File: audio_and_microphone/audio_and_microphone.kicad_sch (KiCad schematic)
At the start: 36 parts, among them J2 Conn_01x02, U1 LM4810, U2 ${SIM.PARAMS}, U3 ${SIM.PARAMS}

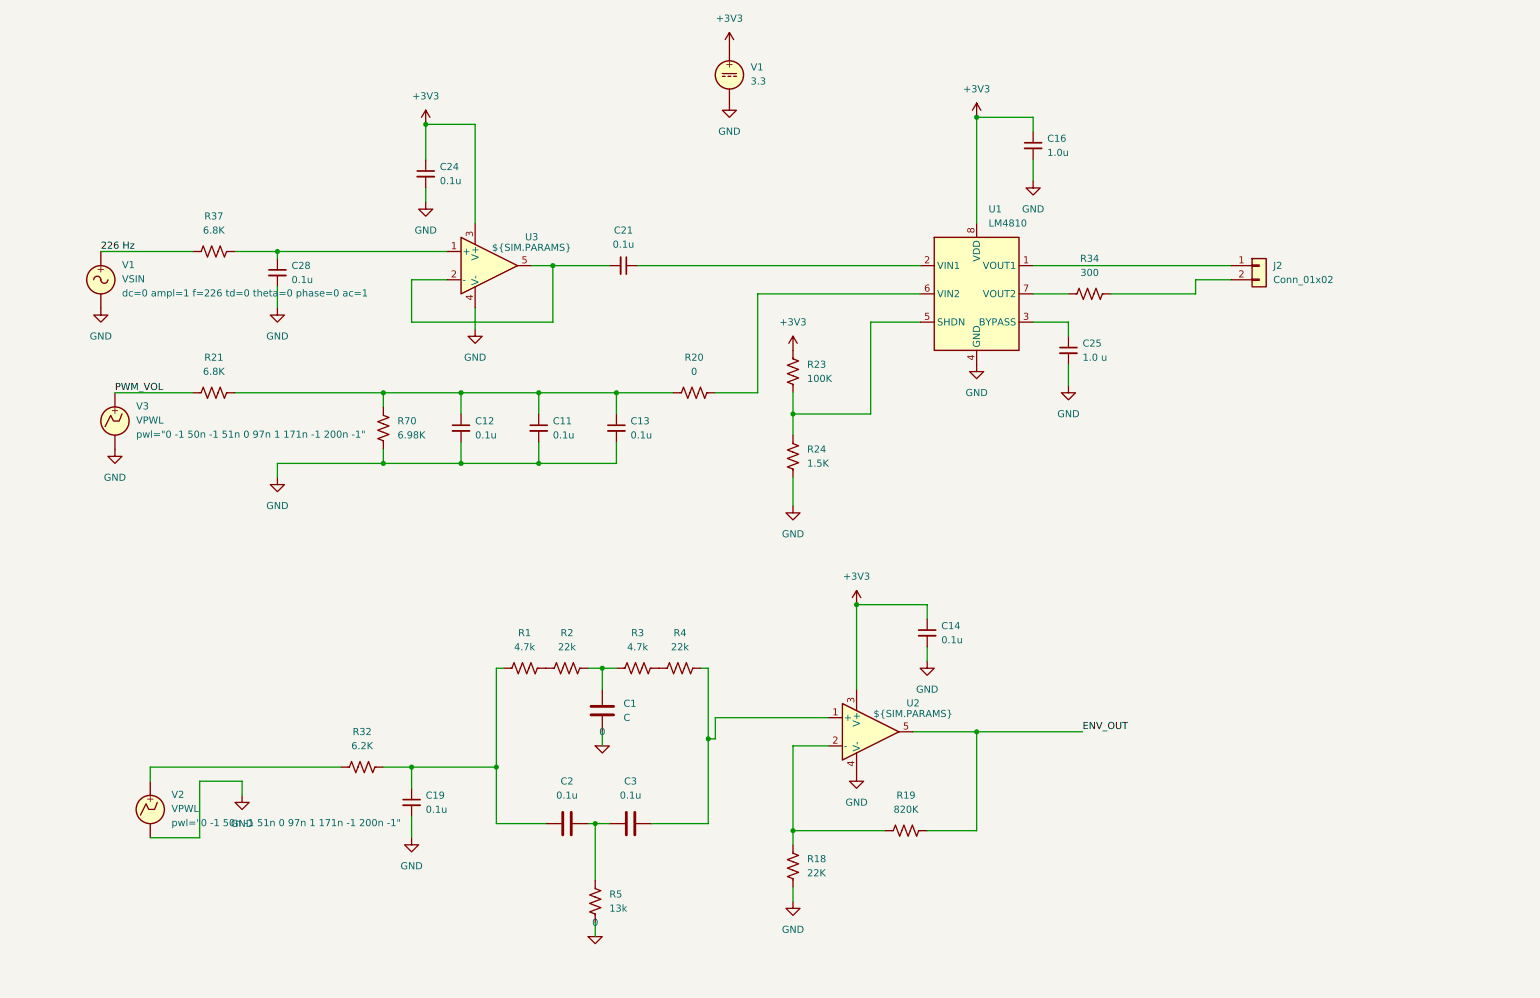
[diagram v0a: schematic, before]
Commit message: assigned footprints and imported SMT designs to pcb layout
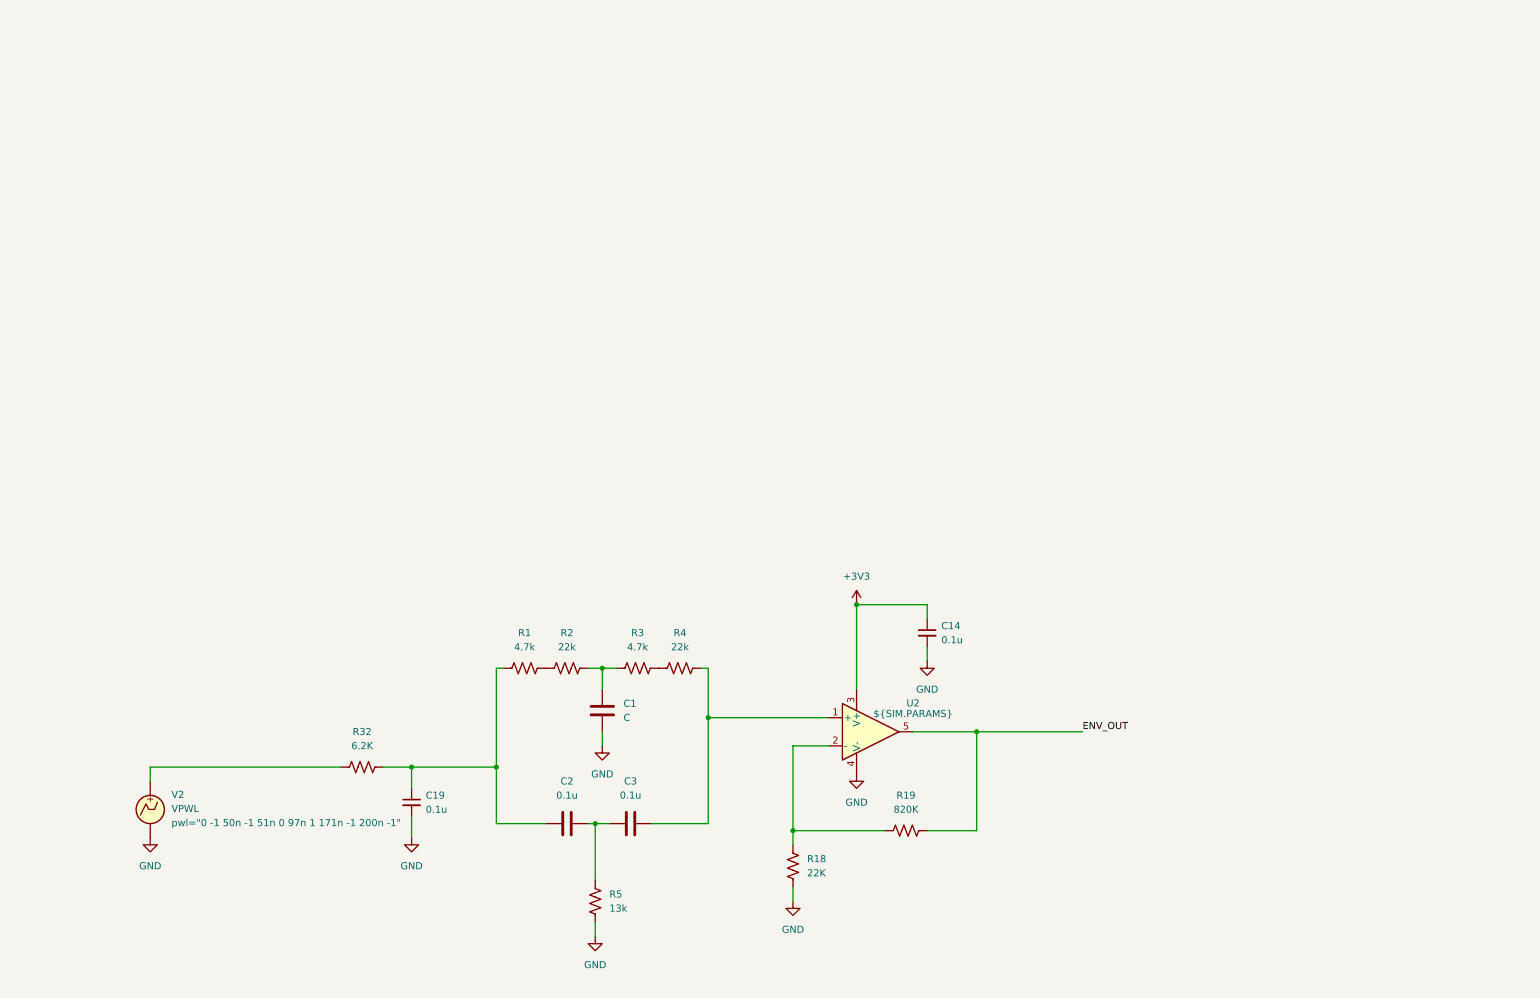
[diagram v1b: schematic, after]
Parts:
- removed C11, C12, C13, C21, C24, C28: 0.1u, symbol Device:C_Small
- removed C16: 1.0u, symbol Device:C_Small
- removed C25: 1.0 u, symbol Device:C_Small
- removed J2: Conn_01x02, symbol Connector_Generic:Conn_01x02
- removed R20: 0, symbol Device:R_US
- removed R21, R37: 6.8K, symbol Device:R_US
- removed R23: 100K, symbol Device:R_US
- removed R24: 1.5K, symbol Device:R_US
- removed R34: 300, symbol Device:R_US
- removed R70: 6.98K, symbol Device:R_US
- removed U1: LM4810, Package_SO:TSSOP-8_3x3mm_P0.65mm, symbol Amplifier_Audio:LM4810
- removed U3: ${SIM.PARAMS}, symbol Simulation_SPICE:OPAMP
- removed V1: VSIN, symbol Simulation_SPICE:VSIN
- removed V1: 3.3, symbol Simulation_SPICE:VDC
- removed V3: VPWL, symbol Simulation_SPICE:VPWL
- C1, C14, C19, C2, C3: footprint (none) -> Capacitor_SMD:C_0201_0603Metric
- R1, R18, R19, R2, R3, R32, R4, R5: footprint (none) -> Resistor_SMD:R_0201_0603Metric
- U2: footprint (none) -> Package_SO:SOIC-8_3.9x4.9mm_P1.27mm
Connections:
- net 0 is gone; now on net GND: C1.2, R5.2

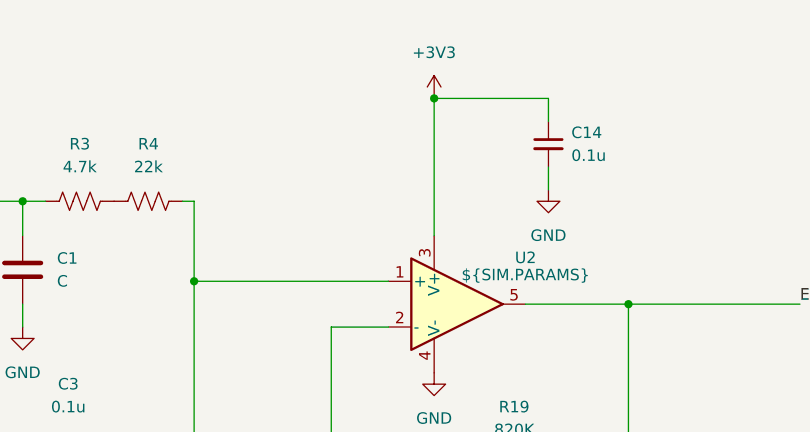
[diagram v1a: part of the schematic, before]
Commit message: updated footprints and pcb layout without 3.3 V connection
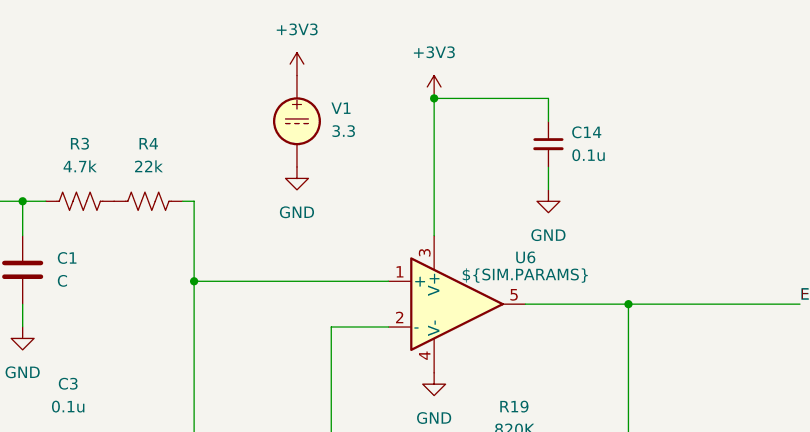
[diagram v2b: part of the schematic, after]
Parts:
- added V1: 3.3, symbol Simulation_SPICE:VDC
- U6: renamed from U2; footprint Package_SO:SOIC-8_3.9x4.9mm_P1.27mm -> Package_TO_SOT_SMD:SOT-23-5
- V2: footprint (none) -> Connector_PinHeader_1.00mm:PinHeader_1x03_P1.00mm_Vertical_SMD_Pin1Left
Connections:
- net +3V3: now also V1.1
- net GND: now also V1.2
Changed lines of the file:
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@@
+	)
+	(symbol
+		(lib_id "Simulation_SPICE:VDC")
+		(at 149.86 123.19 0)
+		(unit 1)
+		(exclude_from_sim no)
+		(in_bom yes)
+		(on_board no)
+		(dnp no)
+		(fields_autoplaced yes)
+		(property "Reference" "V1"
+			(at 153.67 121.7901 0)
+			(effects
+				(font
+					(size 1.27 1.27)
+				)
+				(justify left)
+			)
+		)
+		(property "Value" "3.3"
+			(at 153.67 124.3301 0)
+			(effects
+				(font
+					(size 1.27 1.27)
+				)
+				(justify left)
+			)
+		)
+		(property "Footprint" ""
+			(at 149.86 123.19 0)
+			(effects
+				(font
+					(size 1.27 1.27)
+				)
+				(hide yes)
+			)
+		)
+		(property "Datasheet" "https://ngspice.sourceforge.io/docs/ngspice-html-manual/manual.xhtml#sec_Independent_Sources_for"
+			(at 149.86 123.19 0)
+			(effects
+				(font
+					(size 1.27 1.27)
+				)
+				(hide yes)
+			)
+		)
+		(property "Description" "Voltage source, DC"
+			(at 149.86 123.19 0)
+			(effects
+				(font
+					(size 1.27 1.27)
+				)
+				(hide yes)
+			)
+		)
+		(property "Sim.Pins" "1=+ 2=-"
+			(at 149.86 123.19 0)
+			(effects
+				(font
+					(size 1.27 1.27)
+				)
+				(hide yes)
+			)
+		)
+		(property "Sim.Type" "DC"
+			(at 149.86 123.19 0)
+			(effects
+				(font
+					(size 1.27 1.27)
+				)
+				(hide yes)
+			)
+		)
+		(property "Sim.Device" "V"
+			(at 149.86 123.19 0)
+			(effects
+				(font
+					(size 1.27 1.27)
+				)
+				(justify left)
+				(hide yes)
+			)
+		)
+		(pin "1"
+		)
+		(pin "2"
+		)
+		(instances
+			(project ""
+				(path "/6041ce46-c287-4741-ac80-b7b1d4df1348"
+					(reference "V1")
+					(unit 1)
+				)
+			)
+		)
 	)
 	(symbol
@@
 	)
 	(symbol
+		(lib_id "power:+3.3V")
+		(at 149.86 118.11 0)
+		(unit 1)
+		(exclude_from_sim no)
+		(in_bom yes)
+		(on_board yes)
+		(dnp no)
+		(property "Reference" "#PWR01"
+			(at 149.86 121.92 0)
+			(effects
+				(font
+					(size 1.27 1.27)
+				)
+				(hide yes)
+			)
+		)
+		(property "Value" "+3V3"
+			(at 149.86 113.03 0)
+			(effects
+				(font
+					(size 1.27 1.27)
+				)
+			)
+		)
+		(property "Footprint" ""
+			(at 149.86 118.11 0)
+			(effects
+				(font
+					(size 1.27 1.27)
+				)
+				(hide yes)
+			)
+		)
+		(property "Datasheet" ""
+			(at 149.86 118.11 0)
+			(effects
+				(font
+					(size 1.27 1.27)
+				)
+				(hide yes)
+			)
+		)
+		(property "Description" "Power symbol creates a global label with name \"+3.3V\""
+			(at 149.86 118.11 0)
+			(effects
+				(font
+					(size 1.27 1.27)
+				)
+				(hide yes)
+			)
+		)
+		(pin "1"
+		)
+		(instances
+			(project "audio_and_microphone"
+				(path "/6041ce46-c287-4741-ac80-b7b1d4df1348"
+					(reference "#PWR01")
+					(unit 1)
+				)
+			)
+		)
+	)
+	(symbol
 		(lib_id "power:GND")
 		(at 38.1 162.56 0)
@@
 		(dnp no)
 		(fields_autoplaced yes)
-		(property "Reference" "U2"
+		(property "Reference" "U6"
 			(at 175.26 138.3598 0)
 			(effects
@@
 			)
 		)
-		(property "Footprint" "Package_SO:SOIC-8_3.9x4.9mm_P1.27mm"
+		(property "Footprint" "Package_TO_SOT_SMD:SOT-23-5"
 			(at 167.64 143.51 0)
 			(effects
@@
 			(project ""
 				(path "/6041ce46-c287-4741-ac80-b7b1d4df1348"
-					(reference "U2")
+					(reference "U6")
 					(unit 1)
 				)
@@
 		(exclude_from_sim no)
 		(in_bom yes)
-		(on_board no)
+		(on_board yes)
 		(dnp no)
 		(fields_autoplaced yes)
@@
 			)
 		)
-		(property "Footprint" ""
+		(property "Footprint" "Connector_PinHeader_1.00mm:PinHeader_1x03_P1.00mm_Vertical_SMD_Pin1Left"
 			(at 38.1 157.48 0)
 			(effects
@@
 					(unit 1)
 				)
+			)
+		)
+	)
+	(symbol
+		(lib_id "power:GND")
+		(at 149.86 128.27 0)
+		(unit 1)
+		(exclude_from_sim no)
+		(in_bom yes)
+		(on_board yes)
+		(dnp no)
+		(fields_autoplaced yes)
+		(property "Reference" "#PWR09"
+			(at 149.86 134.62 0)
+			(effects
+				(font
+					(size 1.27 1.27)
+				)
+				(hide yes)
+			)
+		)
+		(property "Value" "GND"
+			(at 149.86 133.35 0)
+			(effects
+				(font
+					(size 1.27 1.27)
+				)
+			)
+		)
+		(property "Footprint" ""
+			(at 149.86 128.27 0)
+			(effects
+				(font
+					(size 1.27 1.27)
+				)
+				(hide yes)
+			)
+		)
+		(property "Datasheet" ""
+			(at 149.86 128.27 0)
+			(effects
+				(font
+					(size 1.27 1.27)
+				)
+				(hide yes)
+			)
+		)
+		(property "Description" "Power symbol creates a global label with name \"GND\" , ground"
+			(at 149.86 128.27 0)
+			(effects
+				(font
+					(size 1.27 1.27)
+				)
+				(hide yes)
+			)
+		)
+		(pin "1"
+		)
+		(instances
+			(project "audio_and_microphone"
+				(path "/6041ce46-c287-4741-ac80-b7b1d4df1348"
+					(reference "#PWR09")
+					(unit 1)
+				)

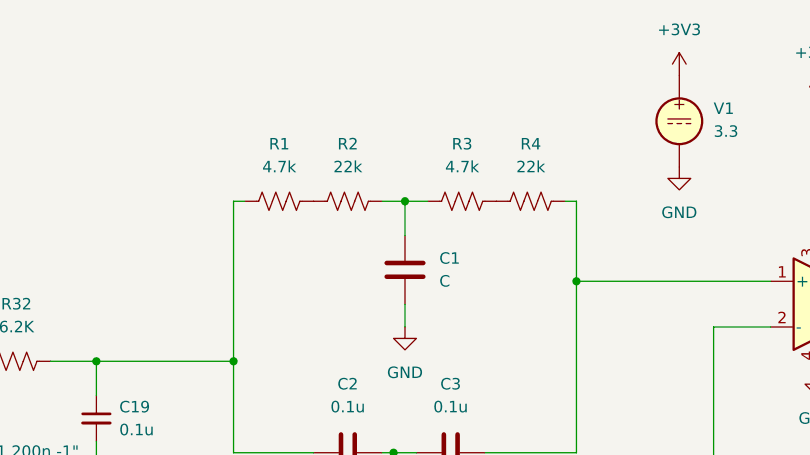
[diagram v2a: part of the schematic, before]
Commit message: excluded voltage sources from board and replaced with connectors
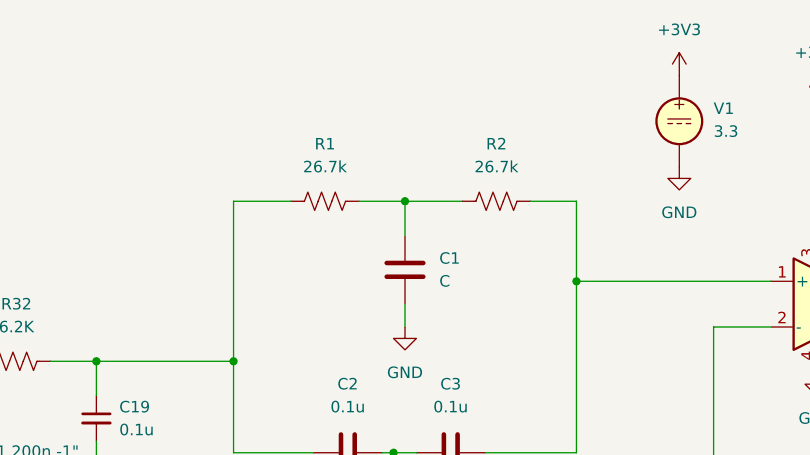
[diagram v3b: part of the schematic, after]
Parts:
- removed R2: 22k, Resistor_SMD:R_0201_0603Metric, symbol Device:R_US
- removed R3: 4.7k, Resistor_SMD:R_0201_0603Metric, symbol Device:R_US
- R1: value 4.7k -> 26.7k
- R2: renamed from R4; value 22k -> 26.7k
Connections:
- net at R1.2: now also C1.1, R2.1
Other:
- moved on the sheet: R1, R2
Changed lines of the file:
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@@
 	(wire
 		(pts
-			(xy 100.33 132.08) (xy 101.6 132.08)
+			(xy 100.33 132.08) (xy 106.68 132.08)
 		)
 		(stroke
@@
 	(wire
 		(pts
-			(xy 137.16 132.08) (xy 138.43 132.08)
+			(xy 133.35 132.08) (xy 138.43 132.08)
 		)
 		(stroke
@@
 	(wire
 		(pts
+			(xy 114.3 132.08) (xy 119.38 132.08)
+		)
+		(stroke
+			(width 0)
+			(type default)
+		)
+	)
+	(wire
+		(pts
 			(xy 138.43 140.97) (xy 160.02 140.97)
 		)
@@
 	(wire
 		(pts
-			(xy 116.84 132.08) (xy 119.38 132.08)
-		)
-		(stroke
-			(width 0)
-			(type default)
-		)
-	)
-	(wire
-		(pts
 			(xy 118.11 160.02) (xy 118.11 170.18)
 		)
@@
 	(wire
 		(pts
-			(xy 119.38 132.08) (xy 121.92 132.08)
+			(xy 119.38 132.08) (xy 125.73 132.08)
 		)
 		(stroke
@@
 	(symbol
 		(lib_id "Device:R_US")
-		(at 105.41 132.08 90)
+		(at 110.49 132.08 90)
 		(unit 1)
 		(exclude_from_sim no)
@@
 		(fields_autoplaced yes)
 		(property "Reference" "R1"
-			(at 105.41 125.73 90)
-			(effects
-				(font
-					(size 1.27 1.27)
-				)
-			)
-		)
-		(property "Value" "4.7k"
-			(at 105.41 128.27 90)
+			(at 110.49 125.73 90)
+			(effects
+				(font
+					(size 1.27 1.27)
+				)
+			)
+		)
+		(property "Value" "26.7k"
+			(at 110.49 128.27 90)
 			(effects
 				(font
@@
 		)
 		(property "Footprint" "Resistor_SMD:R_0201_0603Metric"
-			(at 105.664 131.064 90)
+			(at 110.744 131.064 90)
 			(effects
 				(font
@@
 		)
 		(property "Datasheet" "~"
-			(at 105.41 132.08 0)
+			(at 110.49 132.08 0)
 			(effects
 				(font
@@
 		)
 		(property "Description" "Resistor, US symbol"
-			(at 105.41 132.08 0)
+			(at 110.49 132.08 0)
 			(effects
 				(font
@@
 	)
 	(symbol
-		(lib_id "Device:R_US")
-		(at 113.03 132.08 90)
-		(unit 1)
-		(exclude_from_sim no)
-		(in_bom yes)
-		(on_board yes)
-		(dnp no)
-		(fields_autoplaced yes)
-		(property "Reference" "R2"
-			(at 113.03 125.73 90)
-			(effects
-				(font
-					(size 1.27 1.27)
-				)
-			)
-		)
-		(property "Value" "22k"
-			(at 113.03 128.27 90)
-			(effects
-				(font
-					(size 1.27 1.27)
-				)
-			)
-		)
-		(property "Footprint" "Resistor_SMD:R_0201_0603Metric"
-			(at 113.284 131.064 90)
-			(effects
-				(font
-					(size 1.27 1.27)
-				)
-				(hide yes)
-			)
-		)
-		(property "Datasheet" "~"
-			(at 113.03 132.08 0)
-			(effects
-				(font
-					(size 1.27 1.27)
-				)
-				(hide yes)
-			)
-		)
-		(property "Description" "Resistor, US symbol"
-			(at 113.03 132.08 0)
-			(effects
-				(font
-					(size 1.27 1.27)
-				)
-				(hide yes)
-			)
-		)
-		(pin "2"
-		)
-		(pin "1"
-		)
-		(instances
-			(project "audio_and_microphone"
-				(path "/6041ce46-c287-4741-ac80-b7b1d4df1348"
-					(reference "R2")
-					(unit 1)
-				)
-			)
-		)
-	)
-	(symbol
-		(lib_id "Device:R_US")
-		(at 125.73 132.08 90)
-		(unit 1)
-		(exclude_from_sim no)
-		(in_bom yes)
-		(on_board yes)
-		(dnp no)
-		(fields_autoplaced yes)
-		(property "Reference" "R3"
-			(at 125.73 125.73 90)
-			(effects
-				(font
-					(size 1.27 1.27)
-				)
-			)
-		)
-		(property "Value" "4.7k"
-			(at 125.73 128.27 90)
-			(effects
-				(font
-					(size 1.27 1.27)
-				)
-			)
-		)
-		(property "Footprint" "Resistor_SMD:R_0201_0603Metric"
-			(at 125.984 131.064 90)
-			(effects
-				(font
-					(size 1.27 1.27)
-				)
-				(hide yes)
-			)
-		)
-		(property "Datasheet" "~"
-			(at 125.73 132.08 0)
-			(effects
-				(font
-					(size 1.27 1.27)
-				)
-				(hide yes)
-			)
-		)
-		(property "Description" "Resistor, US symbol"
-			(at 125.73 132.08 0)
-			(effects
-				(font
-					(size 1.27 1.27)
-				)
-				(hide yes)
-			)
-		)
-		(pin "2"
-		)
-		(pin "1"
-		)
-		(instances
-			(project "audio_and_microphone"
-				(path "/6041ce46-c287-4741-ac80-b7b1d4df1348"
-					(reference "R3")
-					(unit 1)
-				)
-			)
-		)
-	)
-	(symbol
 		(lib_id "Simulation_SPICE:VPWL")
 		(at 38.1 157.48 0)
@@
 		(exclude_from_sim no)
 		(in_bom yes)
-		(on_board yes)
+		(on_board no)
 		(dnp no)
 		(fields_autoplaced yes)
@@
 	(symbol
 		(lib_id "Device:R_US")
-		(at 133.35 132.08 90)
-		(unit 1)
-		(exclude_from_sim no)
-		(in_bom yes)
-		(on_board yes)
-		(dnp no)
-		(property "Reference" "R4"
-			(at 133.35 125.73 90)
-			(effects
-				(font
-					(size 1.27 1.27)
-				)
-			)
-		)
-		(property "Value" "22k"
-			(at 133.35 128.27 90)
+		(at 129.54 132.08 90)
+		(unit 1)
+		(exclude_from_sim no)
+		(in_bom yes)
+		(on_board yes)
+		(dnp no)
+		(property "Reference" "R2"
+			(at 129.54 125.73 90)
+			(effects
+				(font
+					(size 1.27 1.27)
+				)
+			)
+		)
+		(property "Value" "26.7k"
+			(at 129.54 128.27 90)
 			(effects
 				(font
@@
 		)
 		(property "Footprint" "Resistor_SMD:R_0201_0603Metric"
-			(at 133.604 131.064 90)
+			(at 129.794 131.064 90)
 			(effects
 				(font
@@
 		)
 		(property "Datasheet" "~"
-			(at 133.35 132.08 0)
+			(at 129.54 132.08 0)
 			(effects
 				(font
@@
 		)
 		(property "Description" "Resistor, US symbol"
-			(at 133.35 132.08 0)
+			(at 129.54 132.08 0)
 			(effects
 				(font
@@
 			(project "audio_and_microphone"
 				(path "/6041ce46-c287-4741-ac80-b7b1d4df1348"
-					(reference "R4")
-					(unit 1)
-				)
+					(reference "R2")
+					(unit 1)
+				)
